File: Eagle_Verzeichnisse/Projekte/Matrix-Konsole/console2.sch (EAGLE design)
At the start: 15 parts, among them J1 DIN5, J2 DIN5, J3 DIN5, J4 DIN5, X2 057-016-1

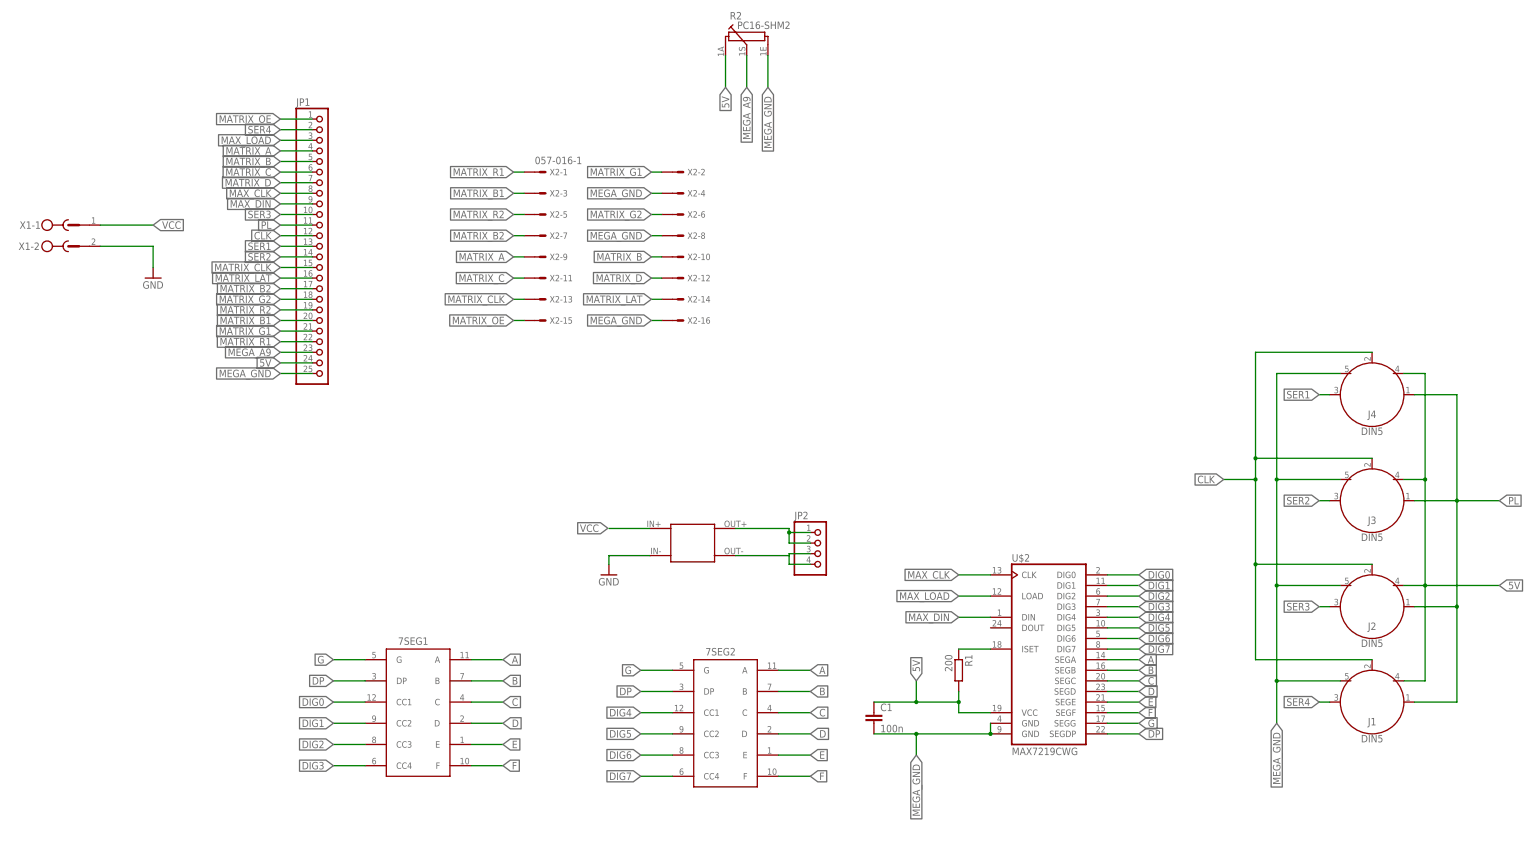
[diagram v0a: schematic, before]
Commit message: Splitted the console-layout into three boards and improved the layouts
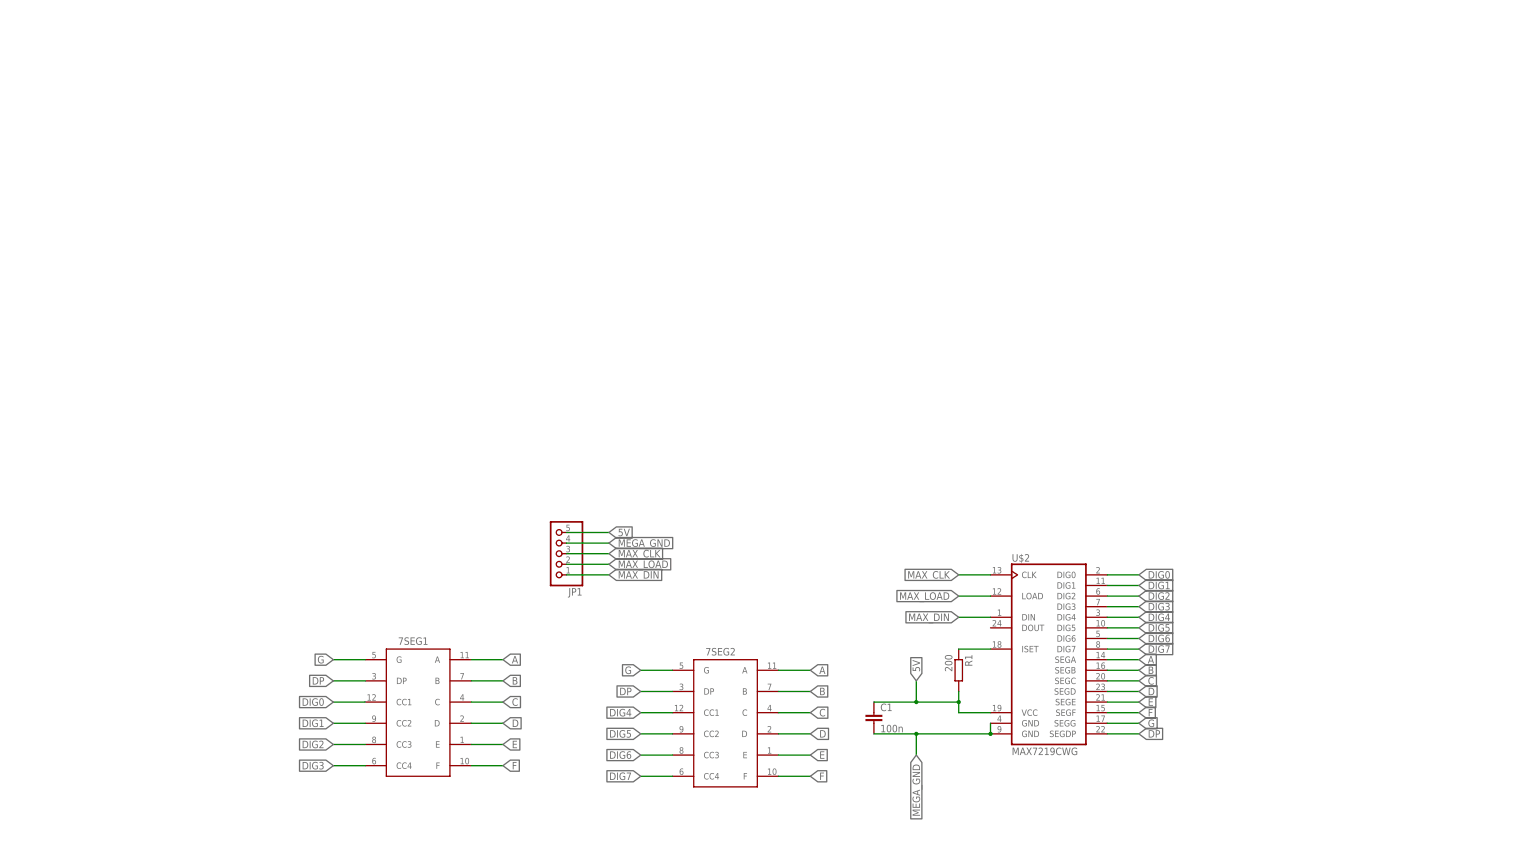
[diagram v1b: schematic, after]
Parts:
- removed J1, J2, J3, J4: DIN5, SparkFun-Connectors:DIN5
- removed JP2: (no value), pinhead:PINHD-1X4
- removed R2: PC16-SHM2, piher:PC16-SHM2
- removed U$1: SPGRGL_DEV, Spannungsregler:SPGRGL_DEV
- removed X1: (no value), con-phoenix-500:MSTBV2
- removed X2: 057-016-1, con-panduit:057-016-1
- JP1: device pinhead:PINHD-1X25 -> pinhead:PINHD-1X5
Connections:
- removed net CLK: J1.2, J2.2, J3.2, J4.2, JP1.12
- removed net GND: U$1.IN-, X1-2.SK
- removed net MATRIX_A: JP1.4, X2-9.S
- removed net MATRIX_B: JP1.5, X2-10.S
- removed net MATRIX_B1: JP1.20, X2-3.S
- removed net MATRIX_B2: JP1.17, X2-7.S
- removed net MATRIX_C: JP1.6, X2-11.S
- removed net MATRIX_CLK: JP1.15, X2-13.S
- removed net MATRIX_D: JP1.7, X2-12.S
- removed net MATRIX_G1: JP1.21, X2-2.S
- removed net MATRIX_G2: JP1.18, X2-6.S
- removed net MATRIX_LAT: JP1.16, X2-14.S
- removed net MATRIX_OE: JP1.1, X2-15.S
- removed net MATRIX_R1: JP1.22, X2-1.S
- removed net MATRIX_R2: JP1.19, X2-5.S
- removed net MEGA_A9: JP1.23, R2G$1.1S
- removed net N$1: JP2.1, JP2.2, U$1.OUT+
- removed net N$8: JP2.3, JP2.4, U$1.OUT-
- removed net PL: J1.1, J2.1, J3.1, J4.1, JP1.11
- removed net SER1: J4.3, JP1.13
- removed net SER2: J3.3, JP1.14
- removed net SER3: J2.3, JP1.10
- removed net SER4: J1.3, JP1.2
- removed net VCC: U$1.IN+, X1-1.SK
- net 5V: now also JP1.5; no longer J1.4, J2.4, J3.4, J4.4, JP1.24, R2G$1.1A
- net MAX_CLK: now also JP1.3; no longer JP1.8
- net MAX_DIN: now also JP1.1; no longer JP1.9
- net MAX_LOAD: now also JP1.2; no longer JP1.3
- net MEGA_GND: now also JP1.4; no longer J1.5, J2.5, J3.5, J4.5, JP1.25, R2G$1.1E, X2-16.S, X2-4.S, X2-8.S
